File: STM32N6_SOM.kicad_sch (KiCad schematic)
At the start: 0 parts

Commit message: PWR STM32 connected, pwr gen to do next
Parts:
- added C18, C48: 100nF, symbol Device:C
- added C46, C47: 1µF, symbol Device:C
- added J1, J2: DF40C-100DP-0.4V_51_, DF40C100DP04V51, symbol SamacSysLib:DF40C-100DP-0.4V_51_
- added U1: STM32N657X0H3Q, C42418080:BGA-264_L14.0-W14.0-STM32N657X0H3Q, symbol PLib:STM32N657X0H3Q
- added Y1: Crystal_GND23, symbol Device:Crystal_GND23
- added Y2: Crystal, symbol Device:Crystal
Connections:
- new net: Y1.2 (G), Y1.3 (G)
- new net GND: C18.2, C46.2, C47.2, C48.2
- new net VDD1V8: C18.1, C48.1, U1.C5 (VDDA18USB), U1.R5 (VDDA18CSI)
- new net VDD3V3: C47.1, U1.A4 (VDD33USB)
- new net VDDCORE: C46.1, U1.R4 (VDDCSI)
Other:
- added sheet PWR (pwr.kicad_sch)
- note added: "Pwr mgmnt, JTAG/SWD, CSI2, SD1/2 USB1/2, recovery UART & GPIOs"
- note added: "SPI1/2, UARTs, I2C4, CAN, TIM1/8 ADC, Audio/network, GPIOs"

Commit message: Power should be OK, memory & clk routing WIP
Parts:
- added C57, C59, C62, C64: 100nF, symbol Device:C
- added C58, C60, C61, C63: 4.7µF, symbol Device:C
- added C65, C66: 8.2pF, symbol Device:C
- added C67, C68: 2.2pF, symbol Device:C
- added R10, R11, R12, R13, R14, R15, R16, R20, R21, R22, R23, R24, R25, R26, R27, R28, R29, R30, R31, R32, R33, R34, R35, R36, R37, R38, R39, R40, R41, R9: 0R, symbol Device:R
- added R17, R18, R19, R8: 10k, symbol Device:R
- added R4, R6, R7: 200, symbol Device:R
- added U4: (no value), symbol PLib:APS256XXN-OBR-BG
- added U5: (no value), symbol PLib:OctoSPI_flash_NOR
- J1, J2: footprint DF40C100DP04V51 -> SamacSys:DF40C100DP04V51
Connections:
- net GND: now also J1.101, J1.102, J1.103, J1.104, Y1.2 (G), Y1.3 (G), C57.2, C58.2, C59.2, C60.2, C61.2, C62.2, C63.2, C64.2, C65.2, C66.2, C67.2, C68.2, R18.2, R4.1, R6.1, R7.1, U4.C1 (VSS_1), U4.E5 (VSS_2), U5.B3 (VSS), U5.C1 (VSS), U5.E5 (VSS)
- net VDD1V8: now also C57.1, C58.1, C59.1, C60.1, C61.1, C62.1, C63.1, C64.1, R17.1, R19.1, R8.1, U4.D1 (VDD_1), U4.E4 (VDD_2), U5.B4 (VDD), U5.D1 (VDD), U5.E4 (VDD)
- net VDD3V3: no longer C47.1, U1.A4 (VDD33USB)
- net PQ6: now reaches U1.A2 (PQ6)
- net PQ3: now reaches U1.D3 (PQ3)
- net PQ4: now reaches U1.D4 (PQ4)
- net PQ5: now reaches U1.D5 (PQ5)
- net PQ2: now reaches U1.E3 (PQ2)
- net PQ1: now reaches U1.E4 (PQ1)
- net PQ0: now reaches U1.E5 (PQ0)
- net PP7: now reaches U1.G15 (PP7)
- net PP7: now also R28.1
- net PP6: now reaches U1.G16 (PP6)
- net PP6: now also R27.1
- net PP0: now reaches U1.G17 (PP0)
- net PP0: now also R21.1
- net PQ7: now reaches U1.G5 (PQ7)
- net PP4: now reaches U1.H15 (PP4)
- net PP4: now also R25.1
- net PP1: now reaches U1.H16 (PP1)
- net PP1: now also R22.1
- net PP15: now reaches U1.H17 (PP15)
- net PP15: now also R29.2
- net PP5: now reaches U1.J14 (PP5)
- net PP5: now also R26.1
- net PP12: now reaches U1.J15 (PP12)
- net PP12: now also R32.2
- net PP3: now reaches U1.J16 (PP3)
- net PP3: now also R24.1
- net PP2: now reaches U1.J17 (PP2)
- net PP2: now also R23.1
- net PP13: now reaches U1.K14 (PP13)
- net PP13: now also R31.2
- net PO5: now reaches U1.K15 (PO5)
- net PO1: now reaches U1.K16 (PO1)
- net PO2: now reaches U1.K17 (PO2)
- net PP11: now reaches U1.L15 (PP11)
- net PP11: now also R33.2
- net PP8: now reaches U1.L16 (PP8)
- net PP8: now also R36.2
- net PP14: now reaches U1.L17 (PP14)
- net PP14: now also R30.2
- net PO3: now reaches U1.M16 (PO3)
- net PO0: now reaches U1.M17 (PO0)
- net PP9: now reaches U1.N14 (PP9)
- net PP9: now also R35.2
- net PP10: now reaches U1.N15 (PP10)
- net PP10: now also R34.2
- net PO4: now reaches U1.N16 (PO4)
- net PN4: now reaches U1.N17 (PN4)
- net PN12: now reaches U1.P14 (PN12)
- net PN6: now reaches U1.P15 (PN6)
- net PN8: now reaches U1.P16 (PN8)
- net PN0: now reaches U1.P17 (PN0)
- net PN3: now reaches U1.R15 (PN3)
- net PN5: now reaches U1.R16 (PN5)
- net PN1: now reaches U1.R17 (PN1)
- net PN9: now reaches U1.T15 (PN9)
- net PN7: now reaches U1.T16 (PN7)
- net PN2: now reaches U1.T17 (PN2)
- net PN10: now reaches U1.U15 (PN10)
- net PN11: now reaches U1.U16 (PN11)
- net at Y2.1: now also C67.1, R41.2
- net at Y2.2: now also C68.1, R40.1
- net PE13: now reaches U1.A11 (PE13)
- net PE15: now reaches U1.A12 (PE15)
- net PE8: now reaches U1.A15 (PE8)
- net PE9: now reaches U1.A16 (PE9)
- net PH0-OSC_IN: now reaches U1.A7 (PH0-OSC_IN)
- net PH0-OSC_IN: now also R39.1
- net PH3: now reaches U1.B1 (PH3)
- net PE14: now reaches U1.B11 (PE14)
- net PE12: now reaches U1.B12 (PE12)
- net PE7: now reaches U1.B13 (PE7)
- net PE10: now reaches U1.B16 (PE10)
- net PH6: now reaches U1.B2 (PH6)
- net PH1-OSC_OUT: now reaches U1.B7 (PH1-OSC_OUT)
- net PH1-OSC_OUT: now also R38.2
- net PE5: now reaches U1.C11 (PE5)
- net PH8: now reaches U1.C2 (PH8)
- net PE4: now reaches U1.D10 (PE4)
- net PE6: now reaches U1.D11 (PE6)
- net PH7: now reaches U1.D2 (PH7)
- net PH9: now reaches U1.D8 (PH9)
- net PE11: now reaches U1.E11 (PE11)
- net PH2: now reaches U1.E7 (PH2)
- net PE3: now reaches U1.F14 (PE3)
- net PE2: now reaches U1.F15 (PE2)
- net PE0: now reaches U1.F16 (PE0)
- net PE1: now reaches U1.F17 (PE1)
- net PH4: now reaches U1.F4 (PH4)
- net PH5: now reaches U1.F5 (PH5)
- net PG7: now reaches U1.L1 (PG7)
- net PF4: now reaches U1.L2 (PF4)
- net PG6: now reaches U1.L3 (PG6)
- net PF10: now reaches U1.L4 (PF10)
- net PF6: now reaches U1.L5 (PF6)
- net PF7: now reaches U1.M1 (PF7)
- net PF3: now reaches U1.M2 (PF3)
- net PF5: now reaches U1.M3 (PF5)
- net PG5: now reaches U1.M4 (PG5)
- net PF15: now reaches U1.N1 (PF15)
- net PF14: now reaches U1.N2 (PF14)
- net PF8: now reaches U1.N3 (PF8)
- net PF2: now reaches U1.N4 (PF2)
- net PF9: now reaches U1.P1 (PF9)
- net PG4: now reaches U1.P2 (PG4)
- net PF11: now reaches U1.P3 (PF11)
- net PF1: now reaches U1.P4 (PF1)
- net PG14: now reaches U1.P6 (PG14)
- net PG3: now reaches U1.R1 (PG3)
- net PG0: now reaches U1.R13 (PG0)
- net PF13: now reaches U1.R2 (PF13)
- net PF0: now reaches U1.R3 (PF0)
- net PG15: now reaches U1.R6 (PG15)
- net PG1: now reaches U1.R9 (PG1)
- net PF12: now reaches U1.T1 (PF12)
- net PG10: now reaches U1.T10 (PG10)
- net PG2: now reaches U1.T11 (PG2)
- net PG9: now reaches U1.T13 (PG9)
- net PG8: now reaches U1.T14 (PG8)
- net PG12: now reaches U1.T9 (PG12)
- net PG11: now reaches U1.U13 (PG11)
- net PG13: now reaches U1.U9 (PG13)
- net PC4: now reaches U1.A10 (PC4)
- net PD10: now reaches U1.A13 (PD10)
- net PD1: now reaches U1.A14 (PD1)
- net PC10: now reaches U1.A8 (PC10)
- net PC1: now reaches U1.A9 (PC1)
- net PC5: now reaches U1.B10 (PC5)
- net PD15: now reaches U1.B14 (PD15)
- net PD4: now reaches U1.B15 (PD4)
- net PB14: now reaches U1.B17 (PB14)
- net PC11: now reaches U1.B8 (PC11)
- net PC6: now reaches U1.B9 (PC6)
- net PC15-OSC32_OUT: now reaches U1.C1 (PC15-OSC32_OUT)
- net PC15-OSC32_OUT: now also R40.2
- net PC0: now reaches U1.C10 (PC0)
- net PD2: now reaches U1.C12 (PD2)
- net PD12: now reaches U1.C13 (PD12)
- net PD14: now reaches U1.C14 (PD14)
- net PB13: now reaches U1.C15 (PB13)
- net PB2: now reaches U1.C16 (PB2)
- net PD13: now reaches U1.C17 (PD13)
- net PC9: now reaches U1.C7 (PC9)
- net PC12: now reaches U1.C8 (PC12)
- net PC7: now reaches U1.C9 (PC7)
- net PC14-OSC32_IN: now reaches U1.D1 (PC14-OSC32_IN)
- net PC14-OSC32_IN: now also R41.1
- net PD6: now reaches U1.D12 (PD6)
- net PD0: now reaches U1.D13 (PD0)
- net PD5: now reaches U1.D14 (PD5)
- net PB9: now reaches U1.D15 (PB9)
- net PB8: now reaches U1.D16 (PB8)
- net PB15: now reaches U1.D17 (PB15)
- net PC8: now reaches U1.D7 (PC8)
- net PC2: now reaches U1.D9 (PC2)
- net PC3: now reaches U1.E10 (PC3)
- net PD7: now reaches U1.E12 (PD7)
- net PD3: now reaches U1.E13 (PD3)
- net PD8: now reaches U1.E14 (PD8)
- net PB0: now reaches U1.E15 (PB0)
- net PB7: now reaches U1.E16 (PB7)
- net PB6: now reaches U1.E17 (PB6)
- net PB3: now reaches U1.F13 (PB3)
- net PC13: now reaches U1.F3 (PC13)
- net PD11: now reaches U1.G14 (PD11)
- net NRST: now reaches U1.G3 (NRST)
- net BOOT0: now reaches U1.G4 (BOOT0)
- net PD9: now reaches U1.H14 (PD9)
- net PB11: now reaches U1.P10 (PB11)
- net PA15: now reaches U1.P12 (PA15)
- net PA9: now reaches U1.P7 (PA9)
- net PA6: now reaches U1.P8 (PA6)
- net PA1: now reaches U1.P9 (PA1)
- net PB12: now reaches U1.R10 (PB12)
- net PB1: now reaches U1.R11 (PB1)
- net PA7: now reaches U1.R12 (PA7)
- net PA3: now reaches U1.R14 (PA3)
- net PA10: now reaches U1.R7 (PA10)
- net PA5: now reaches U1.R8 (PA5)
- net PB4: now reaches U1.T12 (PB4)
- net PA14: now reaches U1.T6 (PA14)
- net PA11: now reaches U1.T7 (PA11)
- net PA2: now reaches U1.T8 (PA2)
- net PA0: now reaches U1.U10 (PA0)
- net PB10: now reaches U1.U11 (PB10)
- net PB5: now reaches U1.U12 (PB5)
- net PA4: now reaches U1.U14 (PA4)
- net PA13: now reaches U1.U6 (PA13)
- net PA12: now reaches U1.U7 (PA12)
- net PA8: now reaches U1.U8 (PA8)
- net at Y1.1: now also C65.1, R39.2
- net at Y1.4: now also C66.1, R38.1
- net at U1.C6 (OTG1_TXRTUNE): now also R7.2
- net at U1.D6 (OTG2_TXRTUNE): now also R6.2
- net at U1.P5 (CSI_REXT): now also R4.2
- net CSI_CKP: now reaches U1.T3 (CSI_CKP)
- net CSI_D1P: now reaches U1.T4 (CSI_D1P)
- net CSI_D0P: now reaches U1.T5 (CSI_D0P)
- net CSI_CKN: now reaches U1.U3 (CSI_CKN)
- net CSI_D1N: now reaches U1.U4 (CSI_D1N)
- net CSI_D0N: now reaches U1.U5 (CSI_D0N)
- new net: R36.1, U4.C2 (DQ8)
- new net: R32.1, U4.A5 (DQ12)
- new net: R9.2, U5.E1 (IO7)
- new net: R34.1, U4.A2 (DQ10)
- new net: R33.1, U4.A4 (DQ11)
- new net: R35.1, U4.B1 (DQ9)
- new net: R37.2, U4.B2 (CLK)
- new net: R31.1, U4.B4 (DQ13)
- new net: R30.1, U4.B5 (DQ14)
- new net: R23.2, U4.C4 (ADQ2)
- new net: R29.1, U4.C5 (DQ15)
- new net: R22.2, U4.D2 (ADQ1)
- new net: R21.2, U4.D3 (ADQ0)
- new net: R24.2, U4.D4 (ADQ3)
- new net: R25.2, U4.D5 (ADQ4)
- new net: R28.2, U4.E1 (ADQ7)
- new net: R27.2, U4.E2 (ADQ6)
- new net: R26.2, U4.E3 (ADQ5)
- new net: R19.2, U5.A5 (ECS#)
- new net: R13.2, U5.D4 (IO3)
- new net: R17.2, R18.1, U5.A4 (RESET#)
- new net: R16.2, U5.D3 (IO0)
- new net: R20.2, U5.B2 (CLK)
- new net: R14.2, U5.C4 (IO2)
- new net: U5.A2 (NC), U5.A3 (NC), U5.B1 (NC), U5.B5 (NC)
- new net: R8.2, U5.C2 (CE#)
- new net: R15.2, U5.D2 (IO1)
- new net: R12.2, U5.D5 (IO4)
- new net: R10.2, U5.E2 (IO6)
- new net: R11.2, U5.E3 (IO5)
- new net VDD3V3_EXT: C47.1, U1.A4 (VDD33USB)
- no-connect marks 0 -> 1
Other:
- moved on the sheet: C18, C46, C47, C48, U1C, U1D, U1F, Y1, Y2

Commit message: Lots of footprint & memory schematic
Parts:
- removed R19: 10k, symbol Device:R
- added R42: 10k, symbol Device:R
- U4: LCSC (none) -> C7420405
- U5: value (none) -> 512Mbit; LCSC (none) -> C20099949
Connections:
- net GND: now also R8.2, R42.1
- net PN0: now also U5.C3 (DQS/DM0)
- net PN10: now also R10.1
- net PN11: now also R9.1
- net PN2: now also R16.1
- net PN3: now also R15.1
- net PN4: now also R14.1
- net PN5: now also R13.1
- net PN6: now also R20.1
- net PN8: now also R12.1
- net PN9: now also R11.1
- net PO2: now also U4.C3 (DQS/DM0)
- net PO3: now also U4.B3 (DQS/DM1)
- net PO4: now also R37.1
- net VDD1V8: no longer R8.1
- net VDD3V3: now also J1.1, J1.2, J1.3, J1.4, J1.5, J1.6
- net at U4.A3 (CE#): now also R42.2
- net at U5.C2 (CE#): now also R8.1; no longer R8.2
- net OTG2_HSDM: now reaches U1.A3 (OTG2_HSDM)
- net OTG1_HSDM: now reaches U1.A5 (OTG1_HSDM)
- net UCPD1_CC1: now reaches U1.A6 (UCPD1_CC1)
- net OTG2_HSDP: now reaches U1.B3 (OTG2_HSDP)
- net OTG1_HSDP: now reaches U1.B5 (OTG1_HSDP)
- net UCPD1_CC2: now reaches U1.B6 (UCPD1_CC2)
- net OTG1_ID: now reaches U1.C3 (OTG1_ID)
- net OTG2_ID: now reaches U1.E6 (OTG2_ID)
- net PA13 renamed PA13_SWDIO
- net PA14 renamed PA14_SWCLK
- net PB13 renamed PB13_TRACE0
- net PB6 renamed PB6_TRACE2
- net PB7 renamed PB7_TRACE3
- net PC8 renamed PC8_TRACE1
- net PD10 renamed PD10_TRACECLK
- no-connect marks 1 -> 2
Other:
- note added: "1V8 domain"

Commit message: Power & memory should be ok, sanity check in progress, routing started (routing first then GPIO set for mezzanine)
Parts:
- removed C18, C48, C57, C59, C62: 100nF, symbol Device:C
- removed C46, C47: 1µF, symbol Device:C
- removed C58, C60, C61: 4.7µF, symbol Device:C
- removed C65: 8.2pF, symbol Device:C
- removed C67: 2.2pF, symbol Device:C
- removed R10, R11, R12, R13, R14, R15, R16, R20, R21, R22, R23, R24, R25, R26, R27, R28, R29, R30, R31, R32, R33, R34, R35, R36, R38, R39, R40, R41, R9: 0R, symbol Device:R
- removed R17, R18, R42, R8: 10k, symbol Device:R
- added C10, C11, C12, C7, C8, C9: 100nF, Capacitor_SMD:C_0201_0603Metric, symbol Device:C
- added C13, C14: 1µF, Capacitor_SMD:C_0201_0603Metric, symbol Device:C
- added C84, C85: 4.7µF, Capacitor_SMD:C_0402_1005Metric, symbol Device:C
- added C86: 8.2pF, Capacitor_SMD:C_0402_1005Metric, symbol Device:C
- added C87: 2.2pF, Capacitor_SMD:C_0402_1005Metric, symbol Device:C
- added R43, R55, R56, R57, R58: 0R, Capacitor_SMD:C_0402_1005Metric, symbol Device:R
- added R53, R54, R59, R60: 10k, Capacitor_SMD:C_0402_1005Metric, symbol Device:R
- C63, C66, C68, R37: footprint (none) -> Capacitor_SMD:C_0402_1005Metric
- C64: value 100nF -> 4.7µF; footprint (none) -> Capacitor_SMD:C_0402_1005Metric
- U1: footprint C42418080:BGA-264_L14.0-W14.0-STM32N657X0H3Q -> SamacSys:BGA264C80P17X17_1400X1400X100
- U4, U5: footprint (none) -> PLib:tfbga24 (6_8mm2)
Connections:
- net GND: now also J1.7, J1.8, C10.2, C11.2, C12.2, C13.2, C14.2, C7.2, C8.2, C84.2, C85.2, C86.2, C87.2, C9.2, R54.1
- net PC14-OSC32_IN: now also R56.1
- net PC15-OSC32_OUT: now also R58.2
- net PH0-OSC_IN: now also R55.1
- net PH1-OSC_OUT: now also R57.2
- net PN1: now also U5.C2 (CE#), R59.1
- net PN10: now also U5.E2 (IO6)
- net PN11: now also U5.E1 (IO7)
- net PN2: now also U5.D3 (IO0)
- net PN3: now also U5.D2 (IO1)
- net PN4: now also U5.C4 (IO2)
- net PN5: now also U5.D4 (IO3)
- net PN6: now also R43.1
- net PN8: now also U5.D5 (IO4)
- net PN9: now also U5.E3 (IO5)
- net PO0: now also U4.A3 (CE#), R60.1
- net PP0: now also U4.D3 (ADQ0)
- net PP1: now also U4.D2 (ADQ1)
- net PP10: now also U4.A2 (DQ10)
- net PP11: now also U4.A4 (DQ11)
- net PP12: now also U4.A5 (DQ12)
- net PP13: now also U4.B4 (DQ13)
- net PP14: now also U4.B5 (DQ14)
- net PP15: now also U4.C5 (DQ15)
- net PP2: now also U4.C4 (ADQ2)
- net PP3: now also U4.D4 (ADQ3)
- net PP4: now also U4.D5 (ADQ4)
- net PP5: now also U4.E3 (ADQ5)
- net PP6: now also U4.E2 (ADQ6)
- net PP7: now also U4.E1 (ADQ7)
- net PP8: now also U4.C2 (DQ8)
- net PP9: now also U4.B1 (DQ9)
- net VDD1V8: now also C10.1, C11.1, C12.1, C7.1, C8.1, C84.1, C85.1, C9.1, R53.2, R59.2, R60.2
- net VDD3V3_EXT: now also C14.1
- net VDDCORE: now also C13.1
- net at Y2.1: now also C87.1, R56.2
- net at C68.1, Y2.2: now also R58.1
- net at Y1.1: now also C86.1, R55.2
- net at U5.A4 (RESET#): now also R53.1, R54.2
- net at C66.1, Y1.4: now also R57.1
- net at U5.B2 (CLK): now also R43.2
- net OTG1_ID: no longer names the net of U1.C3 (OTG1_ID)
- net OTG2_ID: no longer names the net of U1.E6 (OTG2_ID)
- no-connect marks 2 -> 4

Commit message: All components placed, pwr decoupling routing in progress
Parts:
- removed C10, C9: 100nF, Capacitor_SMD:C_0201_0603Metric, symbol Device:C
- removed C63, C64: 4.7µF, Capacitor_SMD:C_0402_1005Metric, symbol Device:C
- removed R37: 0R, Capacitor_SMD:C_0402_1005Metric, symbol Device:R
- removed R60: 10k, Capacitor_SMD:C_0402_1005Metric, symbol Device:R
- removed U4: (no value), PLib:tfbga24 (6_8mm2), symbol PLib:APS256XXN-OBR-BG
- removed Y1: Crystal_GND23, symbol Device:Crystal_GND23
- added C15, C16: 100nF, Capacitor_SMD:C_0201_0603Metric, symbol Device:C
- added C65, C67: 4.7µF, Capacitor_SMD:C_0402_1005Metric, symbol Device:C
- added R38: 0R, Capacitor_SMD:C_0402_1005Metric, symbol Device:R
- added R61, R62: 10k, Capacitor_SMD:C_0402_1005Metric, symbol Device:R
- added U7: (no value), PLib:tfbga24 (6_8mm2), symbol PLib:W958D8NBYA
- added Y3: Crystal_GND24, PLib:C1985871, symbol Device:Crystal_GND24
- R4, R6, R7: footprint (none) -> Resistor_SMD:R_0402_1005Metric
- Y2: footprint (none) -> PLib:C1987116; LCSC (none) -> C1987116
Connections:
- net GND: now also J1.13, J1.14, C15.2, C16.2, C65.2, C67.2, U7.B3 (VSS), U7.C1 (VSSQ), U7.E5 (VSSQ), Y3.2 (G), Y3.4 (G); no longer J1.7, J1.8
- net NRST: now also R53.1, R54.2, U5.A4 (RESET#), R61.1, U7.A4 (RESET#)
- net PO0: now also R62.1, U7.A3 (CS#)
- net PO2: now also U7.C3 (RWDS)
- net PO4: now also R38.1
- net PP0: now also U7.D3 (DQ0)
- net PP1: now also U7.D2 (DQ1)
- net PP2: now also U7.C4 (DQ2)
- net PP3: now also U7.D4 (DQ3)
- net PP4: now also U7.D5 (DQ4)
- net PP5: now also U7.E3 (DQ5)
- net PP6: now also U7.E2 (DQ6)
- net PP7: now also U7.E1 (DQ7)
- net VDD1V8: now also C15.1, C16.1, C65.1, C67.1, R61.2, R62.2, U7.B4 (VCC), U7.D1 (VCCQ), U7.E4 (VCCQ)
- net VDD3V3: now also J1.10, J1.11, J1.12, J1.7, J1.8, J1.9
- net at C66.1, R57.1: now also Y3.3
- net at C86.1, R55.2: now also Y3.1
- new net: U7.A2 (RFU), U7.A5 (RFU), U7.B5 (RFU), U7.C2 (RFU), U7.C5 (RFU)
- new net: R38.2, U7.B2 (CK)
- no-connect marks 4 -> 5

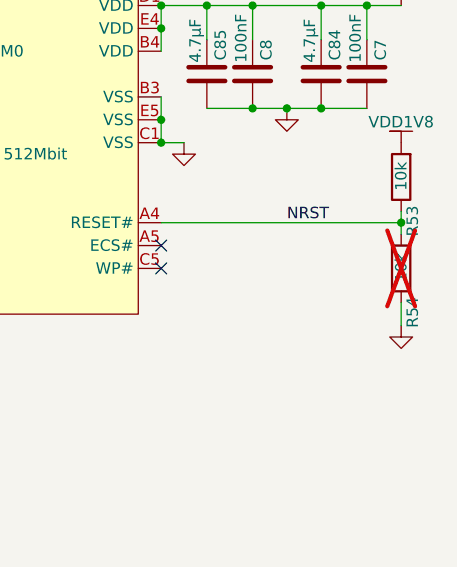
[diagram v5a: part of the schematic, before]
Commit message: Power decoupling done, will work on pwr supplies next then connector routing
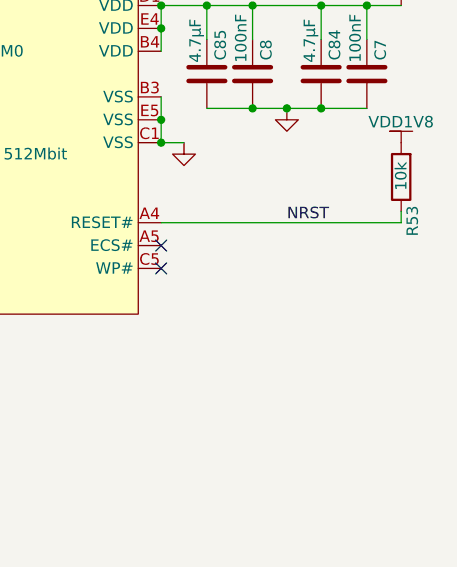
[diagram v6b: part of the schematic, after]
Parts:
- removed R54: 10k, Capacitor_SMD:C_0402_1005Metric, symbol Device:R
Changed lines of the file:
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@@
 	)
 	(junction
-		(at 571.5 128.27)
-		(diameter 0)
-		(color 0 0 0 0)
-	)
-	(junction
 		(at 557.53 77.47)
 		(diameter 0)
@@
 	(wire
 		(pts
-			(xy 571.5 128.27) (xy 571.5 129.54)
-		)
-		(stroke
-			(width 0)
-			(type default)
-		)
-	)
-	(wire
-		(pts
 			(xy 562.61 104.14) (xy 567.69 104.14)
 		)
@@
 	(wire
 		(pts
-			(xy 571.5 139.7) (xy 571.5 137.16)
-		)
-		(stroke
-			(width 0)
-			(type default)
-		)
-	)
-	(wire
-		(pts
 			(xy 189.23 93.98) (xy 203.2 93.98)
 		)
@@
 	)
 	(symbol
-		(lib_id "Device:R")
-		(at 571.5 133.35 180)
-		(unit 1)
-		(body_style 1)
-		(exclude_from_sim no)
-		(in_bom yes)
-		(on_board yes)
-		(in_pos_files yes)
-		(dnp yes)
-		(property "Reference" "R54"
-			(at 572.77 139.954 90)
-			(show_name no)
-			(do_not_autoplace no)
-			(effects
-				(font
-					(size 1.27 1.27)
-				)
-				(justify right)
-			)
-		)
-		(property "Value" "10k"
-			(at 571.5 134.874 90)
-			(show_name no)
-			(do_not_autoplace no)
-			(effects
-				(font
-					(size 1.27 1.27)
-				)
-				(justify right)
-			)
-		)
-		(property "Footprint" "Capacitor_SMD:C_0402_1005Metric"
-			(at 573.278 133.35 90)
-			(hide yes)
-			(show_name no)
-			(do_not_autoplace no)
-			(effects
-				(font
-					(size 1.27 1.27)
-				)
-			)
-		)
-		(property "Datasheet" ""
-			(at 571.5 133.35 0)
-			(hide yes)
-			(show_name no)
-			(do_not_autoplace no)
-			(effects
-				(font
-					(size 1.27 1.27)
-				)
-			)
-		)
-		(property "Description" "Resistor"
-			(at 571.5 133.35 0)
-			(hide yes)
-			(show_name no)
-			(do_not_autoplace no)
-			(effects
-				(font
-					(size 1.27 1.27)
-				)
-			)
-		)
-		(pin "2"
-		)
-		(pin "1"
-		)
-		(instances
-			(project "STM32N6_SOM"
-				(path "/af5ed896-0f4b-4a3b-83a3-1b3549d508f8"
-					(reference "R54")
-					(unit 1)
-				)
-			)
-		)
-	)
-	(symbol
 		(lib_id "Device:C")
 		(at 355.6 162.56 0)
@@
 				)
 			)
-		)
-	)
-	(symbol
-		(lib_id "power:GND")
-		(at 571.5 139.7 0)
-		(unit 1)
-		(body_style 1)
-		(exclude_from_sim no)
-		(in_bom yes)
-		(on_board yes)
-		(in_pos_files yes)
-		(dnp no)
-		(fields_autoplaced yes)
-		(property "Reference" "#PWR062"
-			(at 571.5 146.05 0)
-			(hide yes)
-			(show_name no)
-			(do_not_autoplace no)
-			(effects
-				(font
-					(size 1.27 1.27)
-				)
-			)
-		)
-		(property "Value" "GND"
-			(at 571.5 144.78 0)
-			(hide yes)
-			(show_name no)
-			(do_not_autoplace no)
-			(effects
-				(font
-					(size 1.27 1.27)
-				)
-			)
-		)
-		(property "Footprint" ""
-			(at 571.5 139.7 0)
-			(hide yes)
-			(show_name no)
-			(do_not_autoplace no)
-			(effects
-				(font
-					(size 1.27 1.27)
-				)
-			)
-		)
-		(property "Datasheet" ""
-			(at 571.5 139.7 0)
-			(hide yes)
-			(show_name no)
-			(do_not_autoplace no)
-			(effects
-				(font
-					(size 1.27 1.27)
-				)
-			)
-		)
-		(property "Description" "Power symbol creates a global label with name \"GND\" , ground"
-			(at 571.5 139.7 0)
-			(hide yes)
-			(show_name no)
-			(do_not_autoplace no)
-			(effects
-				(font
-					(size 1.27 1.27)
-				)
-			)
-		)
-		(pin "1"
-		)
-		(instances
-			(project "STM32N6_SOM"
-				(path "/af5ed896-0f4b-4a3b-83a3-1b3549d508f8"
-					(reference "#PWR062")
-					(unit 1)
-				)
-			)
